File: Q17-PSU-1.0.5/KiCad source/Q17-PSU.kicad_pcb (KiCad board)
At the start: 2 copper layers, 102 x 102 mm, 36 parts, among them J1-1 AC1-1, J1-2 AC1-2, J1-3 AC2-1, J1-4 AC2-2, J2-1 V+, J2-2 V+, J2-3 GNDPWR, J2-4 GNDPWR, J2-5 GNDPWR, J2-6 V-, J2-7 V-

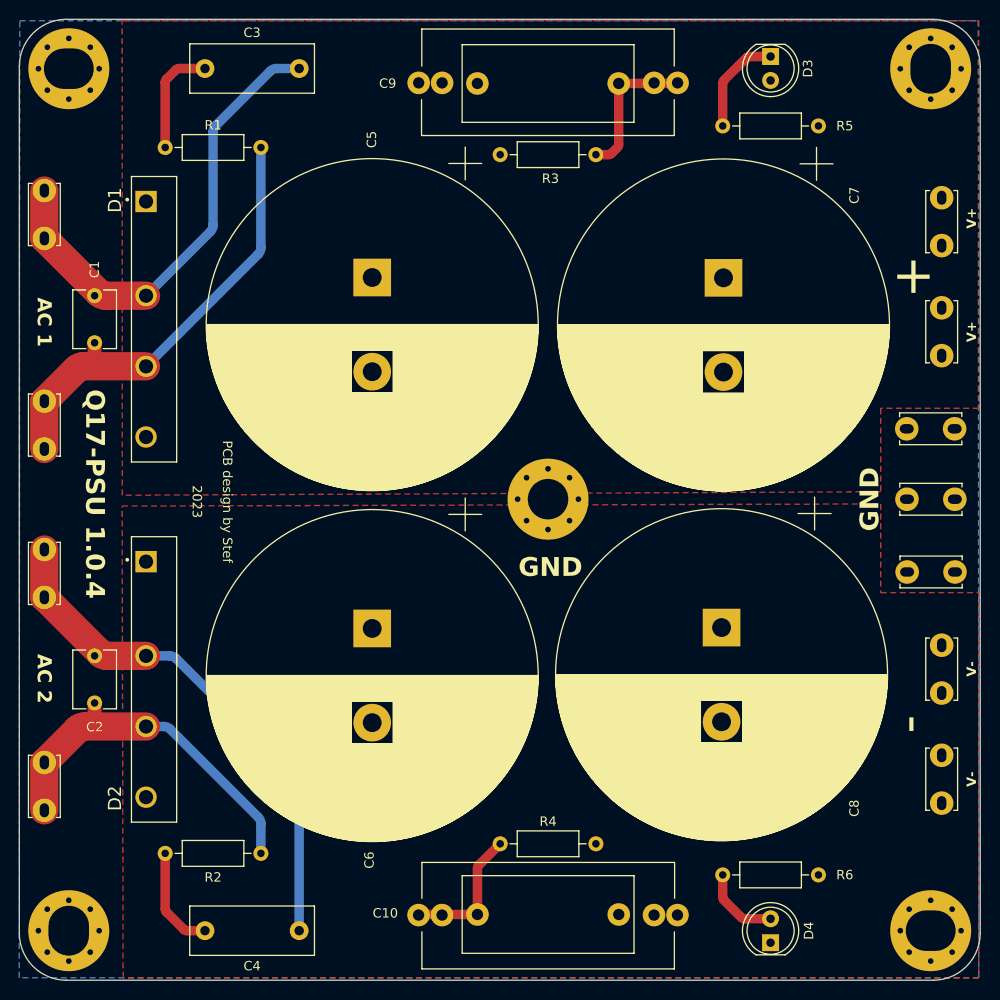
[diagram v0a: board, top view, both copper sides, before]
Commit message: Updated Q17-PSU to 1.0.5
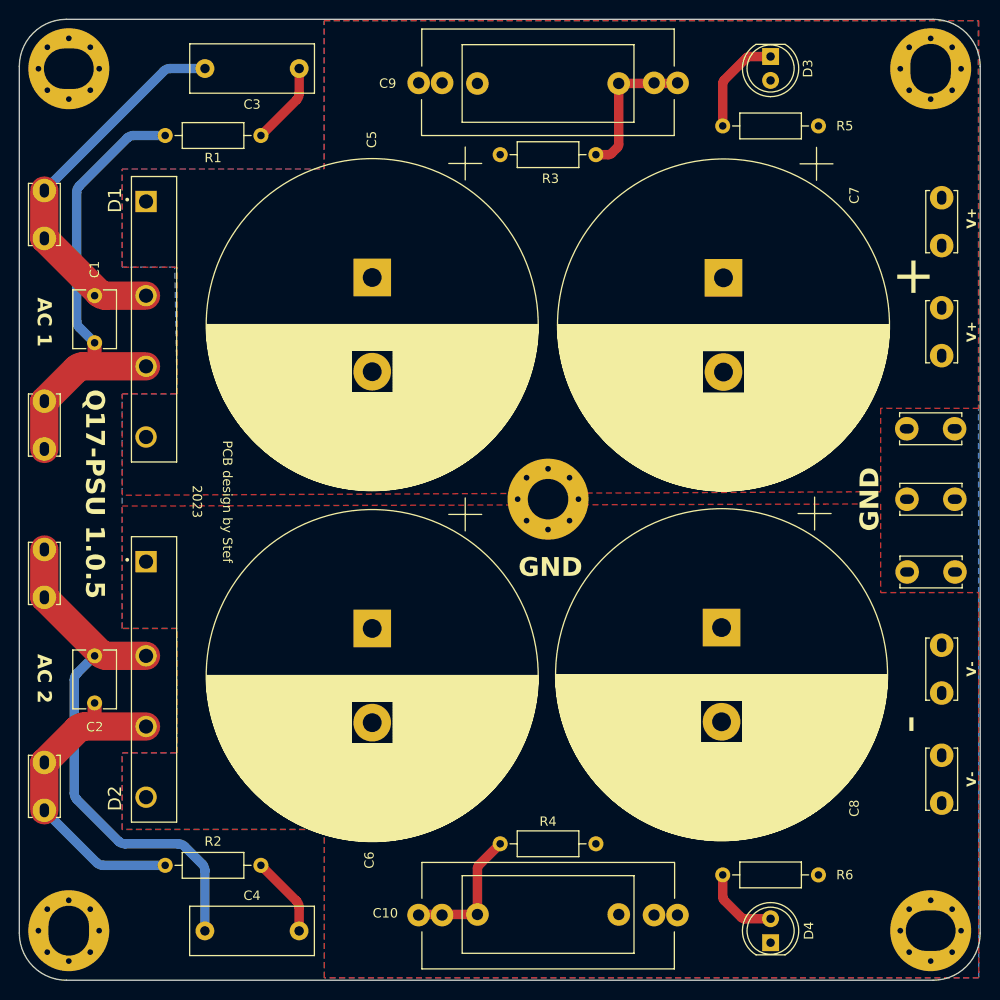
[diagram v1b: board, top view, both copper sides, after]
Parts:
- moved R2 10.2 mm to (123.7, 129.8), turned to 180 degrees
- moved R1 10.2 mm to (123.7, 52.3), turned to 180 degrees
- moved C4 10.0 mm to (117.8, 136.8), turned to 0 degrees
- moved C3 10.0 mm to (117.8, 45.2), turned to 0 degrees
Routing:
- net Net-(J1-1-Pin_1): track 50.7 -> 40.7 mm
- net Net-(J1-4-Pin_1): track 40.1 -> 35.5 mm
- net Net-(C3-Pad2): track 11.8 -> 8.75 mm
- net Net-(C4-Pad2): track 11.1 -> 8.59 mm
- net Net-(J1-3-Pin_1): track 55.9 -> 57.8 mm
- net Net-(J1-2-Pin_1): track 54.9 -> 55.4 mm
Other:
- board text added: "Q17-PSU 1.0.5"
- board text removed: "Q17-PSU 1.0.4"

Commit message: Update Q17-PSU 1.0.5
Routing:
- net Net-(J1-3-Pin_1): track 57.8 -> 56.5 mm
- net Net-(J1-2-Pin_1): track 55.4 -> 56.2 mm
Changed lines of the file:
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@@
   (title_block
     (title "Q17 Power Supply")
-    (date "2023-09-25")
+    (date "2023-09-26")
     (rev "1.0.5")
     (company "by stef")
@@
   (segment (start 107.205435 69.324941) (end 111.506 69.324941) (width 3) (layer "F.Cu") (net 2))
   (segment (start 100.71228 63.246) (end 106.498328 69.032048) (width 3) (layer "F.Cu") (net 2))
+  (segment (start 100.71228 58.166) (end 113.373387 45.504893) (width 1) (layer "F.Cu") (net 2))
+  (segment (start 114.080494 45.212) (end 117.762 45.212) (width 1) (layer "F.Cu") (net 2))
   (segment (start 100.71228 63.246) (end 100.71228 58.166) (width 3) (layer "F.Cu") (net 2))
+  (arc (start 113.373387 45.504893) (mid 113.69781 45.28812) (end 114.080494 45.212) (width 1) (layer "F.Cu") (net 2))
   (arc (start 106.498328 69.032048) (mid 106.822751 69.248821) (end 107.205435 69.324941) (width 3) (layer "F.Cu") (net 2))
-  (segment (start 100.71228 58.166) (end 113.373387 45.504893) (width 1) (layer "B.Cu") (net 2))
-  (segment (start 114.080494 45.212) (end 117.762 45.212) (width 1) (layer "B.Cu") (net 2))
-  (arc (start 113.373387 45.504893) (mid 113.69781 45.28812) (end 114.080494 45.212) (width 1) (layer "B.Cu") (net 2))
   (segment (start 106.630827 107.264547) (end 100.71228 101.346) (width 3) (layer "F.Cu") (net 3))
   (segment (start 100.71228 101.346) (end 100.71228 96.266) (width 3) (layer "F.Cu") (net 3))
   (segment (start 111.506 107.55744) (end 107.337934 107.55744) (width 3) (layer "F.Cu") (net 3))
   (arc (start 106.630827 107.264547) (mid 106.95525 107.48132) (end 107.337934 107.55744) (width 3) (layer "F.Cu") (net 3))
-  (segment (start 103.886 122.115386) (end 103.886 110.131934) (width 1) (layer "B.Cu") (net 3))
-  (segment (start 117.7544 136.7536) (end 117.7544 130.360614) (width 1) (layer "B.Cu") (net 3))
-  (segment (start 104.178893 109.424827) (end 106.04628 107.55744) (width 1) (layer "B.Cu") (net 3))
-  (segment (start 117.461507 129.653507) (end 115.608893 127.800893) (width 1) (layer "B.Cu") (net 3))
-  (segment (start 108.571507 127.215107) (end 104.178893 122.822493) (width 1) (layer "B.Cu") (net 3))
-  (segment (start 114.901786 127.508) (end 109.278614 127.508) (width 1) (layer "B.Cu") (net 3))
-  (arc (start 103.886 122.115386) (mid 103.96212 122.498069) (end 104.178893 122.822493) (width 1) (layer "B.Cu") (net 3))
+  (segment (start 114.053814 136.7536) (end 117.7544 136.7536) (width 1) (layer "B.Cu") (net 3))
+  (segment (start 106.04628 107.55744) (end 104.178893 109.424827) (width 1) (layer "B.Cu") (net 3))
+  (segment (start 104.178893 127.292893) (end 113.346707 136.460707) (width 1) (layer "B.Cu") (net 3))
+  (segment (start 103.886 110.131934) (end 103.886 126.585786) (width 1) (layer "B.Cu") (net 3))
   (arc (start 104.178893 109.424827) (mid 103.96212 109.74925) (end 103.886 110.131934) (width 1) (layer "B.Cu") (net 3))
-  (arc (start 108.571507 127.215107) (mid 108.89593 127.43188) (end 109.278614 127.508) (width 1) (layer "B.Cu") (net 3))
-  (arc (start 115.608893 127.800893) (mid 115.28447 127.58412) (end 114.901786 127.508) (width 1) (layer "B.Cu") (net 3))
-  (arc (start 117.7544 130.360614) (mid 117.67828 129.977931) (end 117.461507 129.653507) (width 1) (layer "B.Cu") (net 3))
+  (arc (start 114.053814 136.7536) (mid 113.671131 136.67748) (end 113.346707 136.460707) (width 1) (layer "B.Cu") (net 3))
+  (arc (start 103.886 126.585786) (mid 103.96212 126.968469) (end 104.178893 127.292893) (width 1) (layer "B.Cu") (net 3))
   (segment (start 100.728887 80.501393) (end 100.71228 80.518) (width 3) (layer "F.Cu") (net 4))
   (segment (start 106.04628 74.324941) (end 106.04628 76.699221) (width 1.5) (layer "F.Cu") (net 4))
@@
   (segment (start 111.506 76.824941) (end 104.819553 76.824941) (width 3) (layer "F.Cu") (net 4))
   (arc (start 104.112446 77.117834) (mid 104.436869 76.901061) (end 104.819553 76.824941) (width 3) (layer "F.Cu") (net 4))
-  (segment (start 109.485907 52.616893) (end 104.432893 57.669907) (width 1) (layer "B.Cu") (net 4))
-  (segment (start 104.14 58.377014) (end 104.14 72.004447) (width 1) (layer "B.Cu") (net 4))
-  (segment (start 113.538 52.324) (end 110.193014 52.324) (width 1) (layer "B.Cu") (net 4))
-  (segment (start 104.432893 72.711554) (end 106.04628 74.324941) (width 1) (layer "B.Cu") (net 4))
-  (arc (start 110.193014 52.324) (mid 109.810331 52.40012) (end 109.485907 52.616893) (width 1) (layer "B.Cu") (net 4))
-  (arc (start 104.14 58.377014) (mid 104.21612 57.994331) (end 104.432893 57.669907) (width 1) (layer "B.Cu") (net 4))
-  (arc (start 104.14 72.004447) (mid 104.21612 72.38713) (end 104.432893 72.711554) (width 1) (layer "B.Cu") (net 4))
+  (segment (start 108.872214 52.324) (end 113.538 52.324) (width 1) (layer "B.Cu") (net 4))
+  (segment (start 104.432893 56.349107) (end 108.165107 52.616893) (width 1) (layer "B.Cu") (net 4))
+  (segment (start 104.14 72.004447) (end 104.14 57.056214) (width 1) (layer "B.Cu") (net 4))
+  (segment (start 106.04628 74.324941) (end 104.432893 72.711554) (width 1) (layer "B.Cu") (net 4))
+  (arc (start 104.432893 56.349107) (mid 104.21612 56.67353) (end 104.14 57.056214) (width 1) (layer "B.Cu") (net 4))
+  (arc (start 104.432893 72.711554) (mid 104.216105 72.387133) (end 104.14 72.004447) (width 1) (layer "B.Cu") (net 4))
+  (arc (start 108.872214 52.324) (mid 108.489531 52.40012) (end 108.165107 52.616893) (width 1) (layer "B.Cu") (net 4))
   (segment (start 111.506 115.05744) (end 104.941054 115.05744) (width 3) (layer "F.Cu") (net 5))
   (segment (start 104.233947 115.350333) (end 100.71228 118.872) (width 3) (layer "F.Cu") (net 5))
+  (segment (start 100.71228 123.952) (end 106.261387 129.501107) (width 1) (layer "F.Cu") (net 5))
   (segment (start 106.04628 114.92916) (end 105.664 115.31144) (width 0.25) (layer "F.Cu") (net 5))
+  (segment (start 106.968494 129.794) (end 113.538 129.794) (width 1) (layer "F.Cu") (net 5))
   (segment (start 100.71228 118.872) (end 100.71228 123.952) (width 3) (layer "F.Cu") (net 5))
   (segment (start 106.04628 112.55744) (end 106.04628 114.92916) (width 1.5) (layer "F.Cu") (net 5))
   (arc (start 104.233947 115.350333) (mid 104.55837 115.13356) (end 104.941054 115.05744) (width 3) (layer "F.Cu") (net 5))
-  (segment (start 100.71228 123.952) (end 106.261387 129.501107) (width 1) (layer "B.Cu") (net 5))
-  (segment (start 106.968494 129.794) (end 113.538 129.794) (width 1) (layer "B.Cu") (net 5))
-  (arc (start 106.968494 129.794) (mid 106.585811 129.71788) (end 106.261387 129.501107) (width 1) (layer "B.Cu") (net 5))
+  (arc (start 106.968494 129.794) (mid 106.585811 129.71788) (end 106.261387 129.501107) (width 1) (layer "F.Cu") (net 5))
   (segment (start 172.866447 46.453833) (end 175.236834 44.083446) (width 1) (layer "F.Cu") (net 6))
   (segment (start 175.590387 43.937) (end 177.8 43.937) (width 1) (layer "F.Cu") (net 6))

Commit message: Update Q17-PSU 1.0.5
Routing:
- net Net-(J1-2-Pin_1): track 56.2 -> 61.1 mm
- net Net-(J1-3-Pin_1): track 56.5 -> 57.3 mm
